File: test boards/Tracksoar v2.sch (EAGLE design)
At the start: 36 parts, among them IC1 BME280, IC2 74AHC1G125DBV, Y1 16MHZ

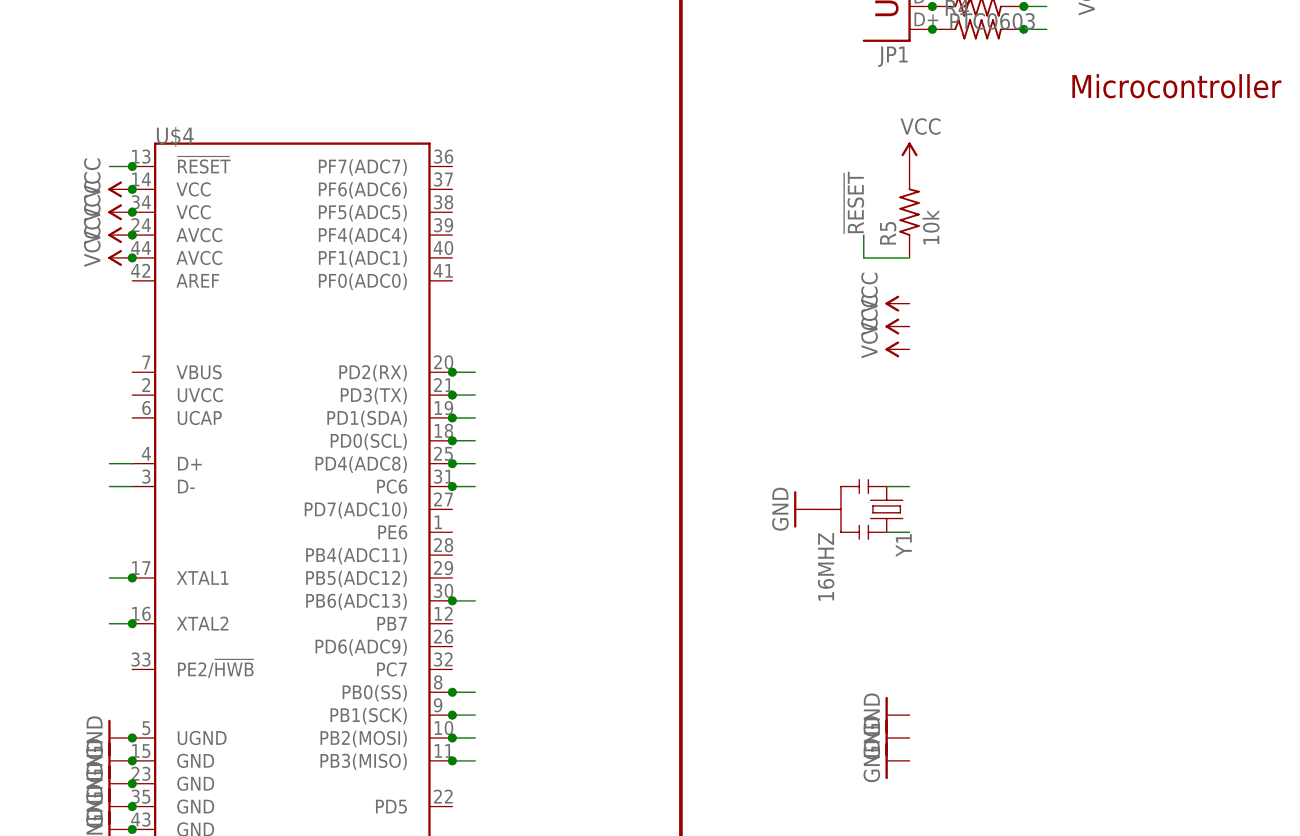
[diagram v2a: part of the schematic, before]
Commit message: tracksoar v2 rev3
added GPIO and analog pins to new header with i2c.
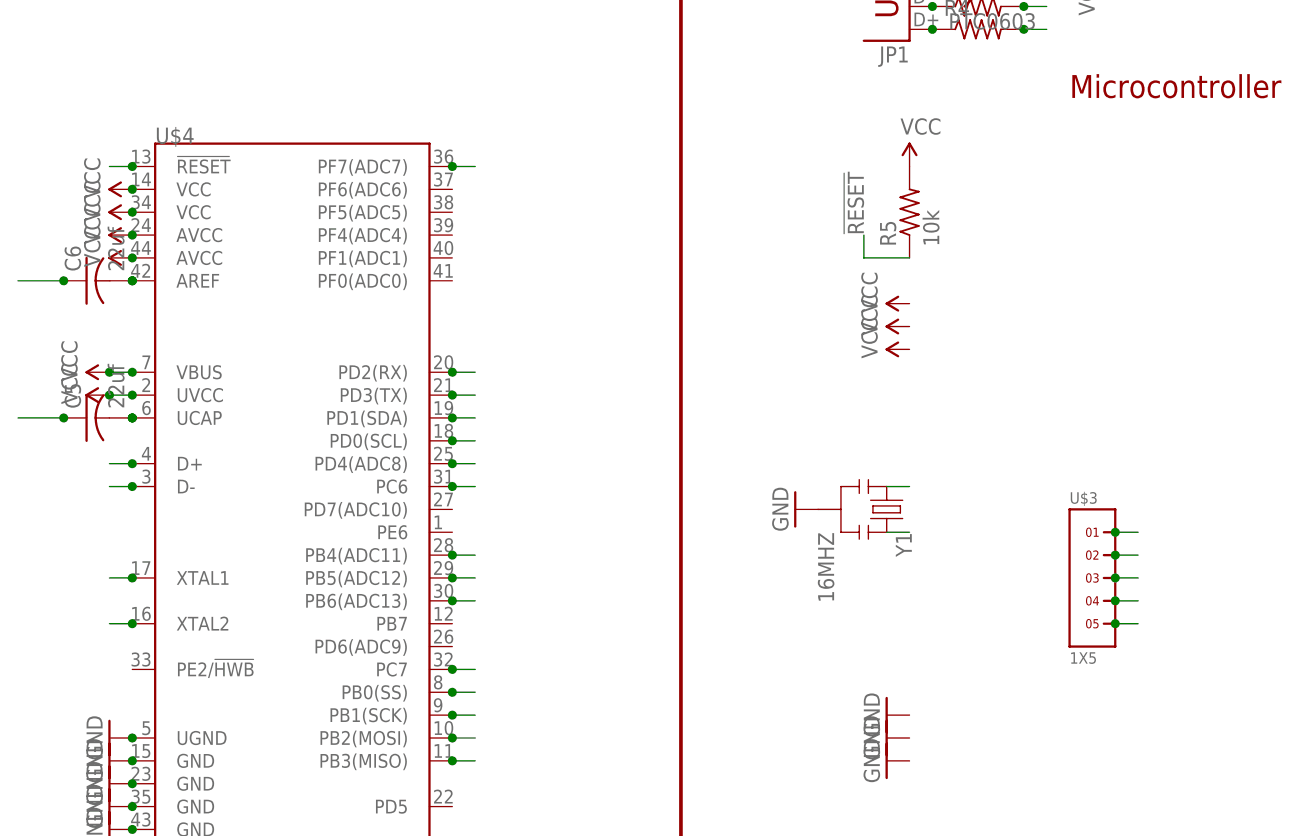
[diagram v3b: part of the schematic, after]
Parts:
- added C5, C6: 22uf, rcl:C-USC0402
- added U$3: 1X5, headers(2mm):1X5
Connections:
- new net A0: U$3.1, U$4.PF7(ADC7)
- new net D13: U$4.PC7
- new net D8: U$3.3, U$4.PB4(ADC11)
- new net D9: U$3.2, U$4.PB5(ADC12)
- new net N$17: C6.2, U$4.AREF
- new net N$20: C5.2, U$4.UCAP
- net GND: now also C5.1, C6.1
- net SCL: now also U$3.4
- net SDA: now also U$3.5
- net VCC: now also U$4.UVCC, U$4.VBUS
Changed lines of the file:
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@@
 <part name="F1" library="SparkFun-PowerIC" deviceset="PTC" device="0603"/>
 <part name="SUPPLY15" library="SparkFun-Aesthetics" deviceset="VCC" device=""/>
+<part name="SUPPLY16" library="SparkFun-Aesthetics" deviceset="VCC" device=""/>
+<part name="SUPPLY17" library="SparkFun-Aesthetics" deviceset="VCC" device=""/>
+<part name="C5" library="rcl" deviceset="C-US" device="C0402" value="22uf"/>
+<part name="C6" library="rcl" deviceset="C-US" device="C0402" value="22uf"/>
+<part name="U$3" library="headers(2mm)" deviceset="1X5" device=""/>
 </parts>
 <sheets>
@@
 <instance part="F1" gate="G$1" x="33.02" y="99.06"/>
 <instance part="SUPPLY15" gate="G$1" x="40.64" y="99.06" rot="R270"/>
+<instance part="SUPPLY16" gate="G$1" x="-63.5" y="55.88" rot="R90"/>
+<instance part="SUPPLY17" gate="G$1" x="-63.5" y="53.34" rot="R90"/>
+<instance part="C5" gate="G$1" x="-66.04" y="50.8" rot="R90"/>
+<instance part="C6" gate="G$1" x="-66.04" y="66.04" rot="R90"/>
+<instance part="U$3" gate="G$1" x="45.72" y="33.02"/>
 </instances>
 <busses>
@@
 <junction x="203.2" y="43.18"/>
 </segment>
+<segment>
+<pinref part="C5" gate="G$1" pin="1"/>
+<wire x1="-68.58" y1="50.8" x2="-73.66" y2="50.8" width="0.1524" layer="91"/>
+<junction x="-68.58" y="50.8"/>
+</segment>
+<segment>
+<pinref part="C6" gate="G$1" pin="1"/>
+<wire x1="-68.58" y1="66.04" x2="-73.66" y2="66.04" width="0.1524" layer="91"/>
+<junction x="-68.58" y="66.04"/>
+</segment>
 </net>
 <net name="D3" class="0">
@@
 <junction x="203.2" y="58.42"/>
 </segment>
+<segment>
+<pinref part="U$4" gate="G$1" pin="VBUS"/>
+<wire x1="-60.96" y1="55.88" x2="-63.5" y2="55.88" width="0.1524" layer="91"/>
+<junction x="-60.96" y="55.88"/>
+<pinref part="SUPPLY16" gate="G$1" pin="VCC"/>
+<junction x="-63.5" y="55.88"/>
+</segment>
+<segment>
+<pinref part="U$4" gate="G$1" pin="UVCC"/>
+<wire x1="-60.96" y1="53.34" x2="-63.5" y2="53.34" width="0.1524" layer="91"/>
+<junction x="-60.96" y="53.34"/>
+<pinref part="SUPPLY17" gate="G$1" pin="VCC"/>
+<junction x="-63.5" y="53.34"/>
+</segment>
 </net>
 <net name="3V" class="0">
@@
 <junction x="-25.4" y="50.8"/>
 </segment>
+<segment>
+<pinref part="U$3" gate="G$1" pin="5"/>
+<wire x1="48.26" y1="27.94" x2="50.8" y2="27.94" width="0.1524" layer="91"/>
+<junction x="48.26" y="27.94"/>
+</segment>
 </net>
 <net name="SCL" class="0">
@@
 <pinref part="U$4" gate="G$1" pin="PD0(SCL)"/>
 <junction x="-25.4" y="48.26"/>
+</segment>
+<segment>
+<pinref part="U$3" gate="G$1" pin="4"/>
+<wire x1="48.26" y1="30.48" x2="50.8" y2="30.48" width="0.1524" layer="91"/>
+<junction x="48.26" y="30.48"/>
 </segment>
 </net>
@@
 <pinref part="U$4" gate="G$1" pin="D+"/>
 <wire x1="-60.96" y1="45.72" x2="-63.5" y2="45.72" width="0.1524" layer="91"/>
+<junction x="-60.96" y="45.72"/>
 </segment>
 </net>
@@
 <pinref part="U$4" gate="G$1" pin="D-"/>
 <wire x1="-60.96" y1="43.18" x2="-63.5" y2="43.18" width="0.1524" layer="91"/>
+<junction x="-60.96" y="43.18"/>
 </segment>
 </net>
@@
 </segment>
 </net>
+<net name="N$20" class="0">
+<segment>
+<pinref part="U$4" gate="G$1" pin="UCAP"/>
+<junction x="-60.96" y="50.8"/>
+<pinref part="C5" gate="G$1" pin="2"/>
+<junction x="-60.96" y="50.8"/>
+</segment>
+</net>
+<net name="N$17" class="0">
+<segment>
+<pinref part="U$4" gate="G$1" pin="AREF"/>
+<pinref part="C6" gate="G$1" pin="2"/>
+<junction x="-60.96" y="66.04"/>
+<junction x="-60.96" y="66.04"/>
+</segment>
+</net>
+<net name="D8" class="0">
+<segment>
+<pinref part="U$4" gate="G$1" pin="PB4(ADC11)"/>
+<wire x1="-25.4" y1="35.56" x2="-22.86" y2="35.56" width="0.1524" layer="91"/>
+<junction x="-25.4" y="35.56"/>
+</segment>
+<segment>
+<pinref part="U$3" gate="G$1" pin="3"/>
+<wire x1="48.26" y1="33.02" x2="50.8" y2="33.02" width="0.1524" layer="91"/>
+<junction x="48.26" y="33.02"/>
+</segment>
+</net>
+<net name="D9" class="0">
+<segment>
+<pinref part="U$4" gate="G$1" pin="PB5(ADC12)"/>
+<wire x1="-25.4" y1="33.02" x2="-22.86" y2="33.02" width="0.1524" layer="91"/>
+<junction x="-25.4" y="33.02"/>
+</segment>
+<segment>
+<pinref part="U$3" gate="G$1" pin="2"/>
+<wire x1="48.26" y1="35.56" x2="50.8" y2="35.56" width="0.1524" layer="91"/>
+<junction x="48.26" y="35.56"/>
+</segment>
+</net>
+<net name="D13" class="0">
+<segment>
+<pinref part="U$4" gate="G$1" pin="PC7"/>
+<wire x1="-25.4" y1="22.86" x2="-22.86" y2="22.86" width="0.1524" layer="91"/>
+<junction x="-25.4" y="22.86"/>
+</segment>
+</net>
+<net name="A0" class="0">
+<segment>
+<pinref part="U$4" gate="G$1" pin="PF7(ADC7)"/>
+<wire x1="-25.4" y1="78.74" x2="-22.86" y2="78.74" width="0.1524" layer="91"/>
+<junction x="-25.4" y="78.74"/>
+</segment>
+<segment>
+<pinref part="U$3" gate="G$1" pin="1"/>
+<wire x1="48.26" y1="38.1" x2="50.8" y2="38.1" width="0.1524" layer="91"/>
+<junction x="48.26" y="38.1"/>
+</segment>
+</net>

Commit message: tracksoar v2 rev4
fixed routing issues on ground, cleaned up schematic to remove overlaps
and moved items to their proper area of the schematic.
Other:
- note removed: "Serial Jumpers"
- moved on the sheet: C5, C6, F1, JP1, R11, R4, R5, U$3, U$4, Y1

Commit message: tracksoar v2 rev5
added ferrite to 5v output on boost converter. Added 4.7k resistor
between Vin and AREF to provide battery voltage monitoring.
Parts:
- removed C6: 22uf, rcl:C-USC0402
- added L1: BLM15HB121SN1, inductors:BLM15HB121SN1
- added R12: 4.7k, adafruit:R-US_R0402
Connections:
- new net N$19: C7.1, D1.C, L1.1, LT3426.VOUT, R9.2
- net 15V: now also R12.1
- net GND: no longer C6.1
- net N$17: now also R12.2; no longer C6.2
- net VCC: now also L1.2; no longer C7.1, D1.C, LT3426.VOUT, R9.2
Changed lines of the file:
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@@
 <part name="SUPPLY16" library="SparkFun-Aesthetics" deviceset="VCC" device=""/>
 <part name="C5" library="rcl" deviceset="C-US" device="C0402" value="22uf"/>
-<part name="C6" library="rcl" deviceset="C-US" device="C0402" value="22uf"/>
 <part name="U$3" library="headers(2mm)" deviceset="1X5" device=""/>
+<part name="R12" library="adafruit" deviceset="R-US_" device="R0402" value="4.7k"/>
+<part name="L1" library="inductors" deviceset="BLM15H" device="" technology="B121SN1"/>
 </parts>
 <sheets>
@@
 <instance part="R7" gate="G$1" x="137.16" y="48.26" rot="R270"/>
 <instance part="GND27" gate="1" x="30.48" y="119.38"/>
-<instance part="SUPPLY1" gate="G$1" x="66.04" y="137.16" rot="R270"/>
+<instance part="SUPPLY1" gate="G$1" x="63.5" y="137.16" rot="R270"/>
 <instance part="LT3426" gate="G$1" x="30.48" y="134.62"/>
 <instance part="D1" gate="G$1" x="33.02" y="147.32"/>
@@
 <instance part="SUPPLY16" gate="G$1" x="17.78" y="63.5" rot="R90"/>
 <instance part="C5" gate="G$1" x="7.62" y="58.42" rot="R90"/>
-<instance part="C6" gate="G$1" x="15.24" y="73.66" rot="R90"/>
 <instance part="U$3" gate="G$1" x="200.66" y="81.28"/>
+<instance part="R12" gate="G$1" x="15.24" y="73.66"/>
+<instance part="L1" gate="G$1" x="58.42" y="137.16"/>
 </instances>
 <busses>
@@
 <junction x="5.08" y="58.42"/>
 </segment>
-<segment>
-<pinref part="C6" gate="G$1" pin="1"/>
-<wire x1="12.7" y1="73.66" x2="7.62" y2="73.66" width="0.1524" layer="91"/>
-<junction x="12.7" y="73.66"/>
-<label x="5.08" y="73.66" size="1.778" layer="95"/>
-</segment>
 </net>
 <net name="D3" class="0">
@@
 <pinref part="SUPPLY10" gate="G$1" pin="VCC"/>
 <junction x="17.78" y="96.52"/>
-</segment>
-<segment>
-<pinref part="LT3426" gate="G$1" pin="VOUT"/>
-<pinref part="SUPPLY1" gate="G$1" pin="VCC"/>
-<pinref part="D1" gate="G$1" pin="C"/>
-<wire x1="66.04" y1="137.16" x2="53.34" y2="137.16" width="0.1524" layer="91"/>
-<wire x1="53.34" y1="137.16" x2="48.26" y2="137.16" width="0.1524" layer="91"/>
-<wire x1="48.26" y1="137.16" x2="45.72" y2="137.16" width="0.1524" layer="91"/>
-<wire x1="35.56" y1="147.32" x2="45.72" y2="147.32" width="0.1524" layer="91"/>
-<wire x1="45.72" y1="147.32" x2="45.72" y2="137.16" width="0.1524" layer="91"/>
-<pinref part="R9" gate="G$1" pin="2"/>
-<junction x="48.26" y="137.16"/>
-<junction x="45.72" y="137.16"/>
-<junction x="35.56" y="147.32"/>
-<pinref part="C7" gate="G$1" pin="1"/>
-<junction x="53.34" y="137.16"/>
-<junction x="66.04" y="137.16"/>
 </segment>
 <segment>
@@
 <junction x="20.32" y="60.96"/>
 </segment>
+<segment>
+<pinref part="L1" gate="G$1" pin="2"/>
+<pinref part="SUPPLY1" gate="G$1" pin="VCC"/>
+<junction x="63.5" y="137.16"/>
+</segment>
 </net>
 <net name="3V" class="0">
@@
 <junction x="40.64" y="172.72"/>
 </segment>
+<segment>
+<pinref part="R12" gate="G$1" pin="1"/>
+<wire x1="10.16" y1="73.66" x2="7.62" y2="73.66" width="0.1524" layer="91"/>
+<junction x="10.16" y="73.66"/>
+</segment>
 </net>
 <net name="N$9" class="0">
@@
 </segment>
 </net>
-<net name="N$17" class="0">
-<segment>
-<pinref part="U$4" gate="G$1" pin="AREF"/>
-<pinref part="C6" gate="G$1" pin="2"/>
-<junction x="20.32" y="73.66"/>
-<junction x="20.32" y="73.66"/>
-</segment>
-</net>
 <net name="D8" class="0">
 <segment>
@@
 </segment>
 </net>
+<net name="N$17" class="0">
+<segment>
+<pinref part="U$4" gate="G$1" pin="AREF"/>
+<pinref part="R12" gate="G$1" pin="2"/>
+<junction x="20.32" y="73.66"/>
+</segment>
+</net>
+<net name="N$19" class="0">
+<segment>
+<pinref part="LT3426" gate="G$1" pin="VOUT"/>
+<pinref part="D1" gate="G$1" pin="C"/>
+<wire x1="53.34" y1="137.16" x2="48.26" y2="137.16" width="0.1524" layer="91"/>
+<wire x1="48.26" y1="137.16" x2="45.72" y2="137.16" width="0.1524" layer="91"/>
+<wire x1="35.56" y1="147.32" x2="45.72" y2="147.32" width="0.1524" layer="91"/>
+<wire x1="45.72" y1="147.32" x2="45.72" y2="137.16" width="0.1524" layer="91"/>
+<pinref part="R9" gate="G$1" pin="2"/>
+<junction x="48.26" y="137.16"/>
+<junction x="45.72" y="137.16"/>
+<junction x="35.56" y="147.32"/>
+<pinref part="C7" gate="G$1" pin="1"/>
+<pinref part="L1" gate="G$1" pin="1"/>
+<junction x="53.34" y="137.16"/>
+</segment>
+</net>
